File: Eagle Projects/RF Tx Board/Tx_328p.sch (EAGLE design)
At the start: 46 parts, among them Q3 16MHz, Q4 16MHz, U1 ATMEGA328P_TQFP, U2 MCP2551

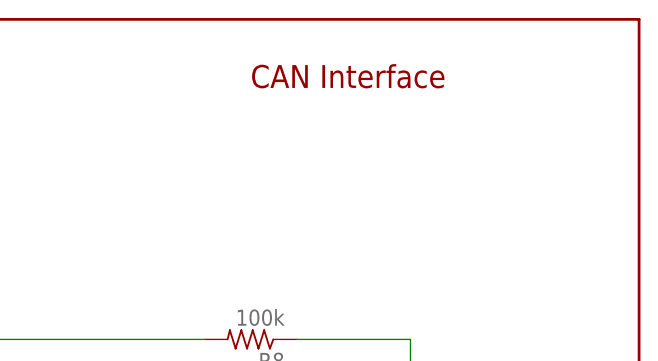
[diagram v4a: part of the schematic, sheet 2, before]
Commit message: Some routing done on Tx board
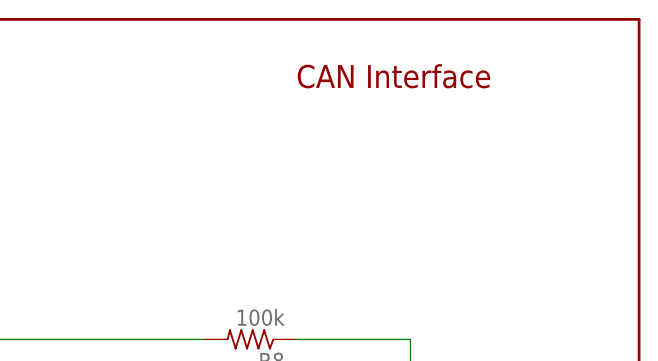
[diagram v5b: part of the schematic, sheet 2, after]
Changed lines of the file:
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@@
 <part name="S1" library="switch" deviceset="SKHMP*E010" device="" technology="S"/>
 <part name="RESET" library="SparkFun-Retired" deviceset="TAC_SWITCH" device="SMD" value="TAC_SWITCHSMD"/>
+<part name="VCC" library="pinhead" deviceset="PINHD-1X1" device=""/>
+<part name="GND" library="pinhead" deviceset="PINHD-1X1" device=""/>
+<part name="GND_2" library="pinhead" deviceset="PINHD-1X1" device=""/>
+<part name="VIN" library="pinhead" deviceset="PINHD-1X1" device=""/>
+<part name="GND16" library="supply1" deviceset="GND" device=""/>
+<part name="GND17" library="supply1" deviceset="GND" device=""/>
+<part name="P+13" library="supply1" deviceset="VCC" device=""/>
 <part name="U$1" library="RobThePyro" deviceset="MCP2515" device="SO"/>
 <part name="U2" library="SparkFun" deviceset="MCP2551" device=""/>
@@
 <part name="Z2" library="supressor" deviceset="TVS-UD-" device="SOD323"/>
 <part name="GND15" library="supply1" deviceset="GND" device=""/>
-<part name="VCC" library="pinhead" deviceset="PINHD-1X1" device=""/>
-<part name="GND" library="pinhead" deviceset="PINHD-1X1" device=""/>
-<part name="GND_2" library="pinhead" deviceset="PINHD-1X1" device=""/>
-<part name="VIN" library="pinhead" deviceset="PINHD-1X1" device=""/>
-<part name="GND16" library="supply1" deviceset="GND" device=""/>
-<part name="GND17" library="supply1" deviceset="GND" device=""/>
-<part name="P+13" library="supply1" deviceset="VCC" device=""/>
 </parts>
 <sheets>
@@
 <wire x1="119.38" y1="-30.48" x2="119.38" y2="60.96" width="0.3048" layer="94"/>
 <wire x1="119.38" y1="60.96" x2="-58.42" y2="60.96" width="0.3048" layer="94"/>
-<text x="76.2" y="53.34" size="2.54" layer="94">CAN Interface</text>
+<text x="81.28" y="53.34" size="2.54" layer="94">CAN Interface</text>
 </plain>
 <instances>

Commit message: Tidy up both boards
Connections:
- net +5V: no longer C7.2, C8.2, R4.2, R5.2, R6.2, U$1G$2.VDD, U2.VDD
- net VCC: now also C7.2, C8.2, R4.2, R5.2, R6.2, U$1G$2.VDD, U2.VDD

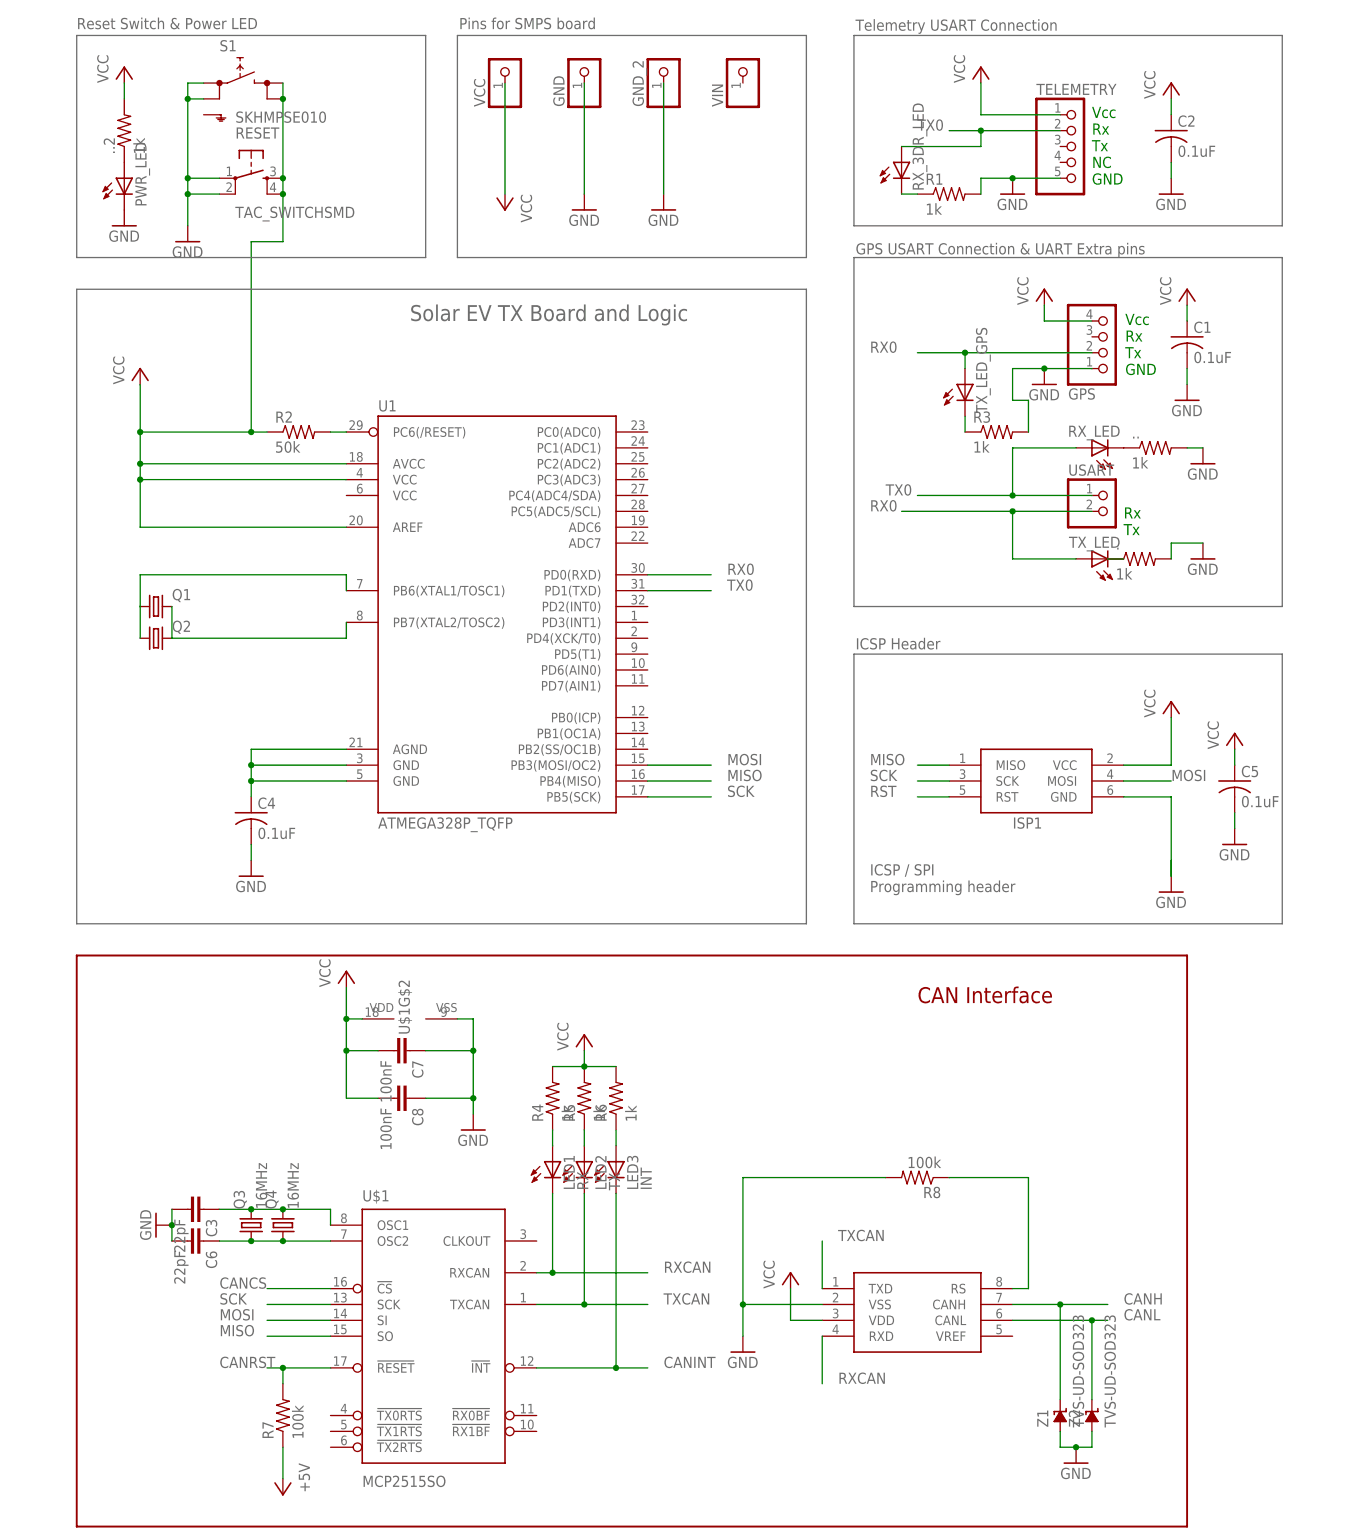
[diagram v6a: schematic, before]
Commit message: More board edits, nearly done routing (actual neatness is debatable)
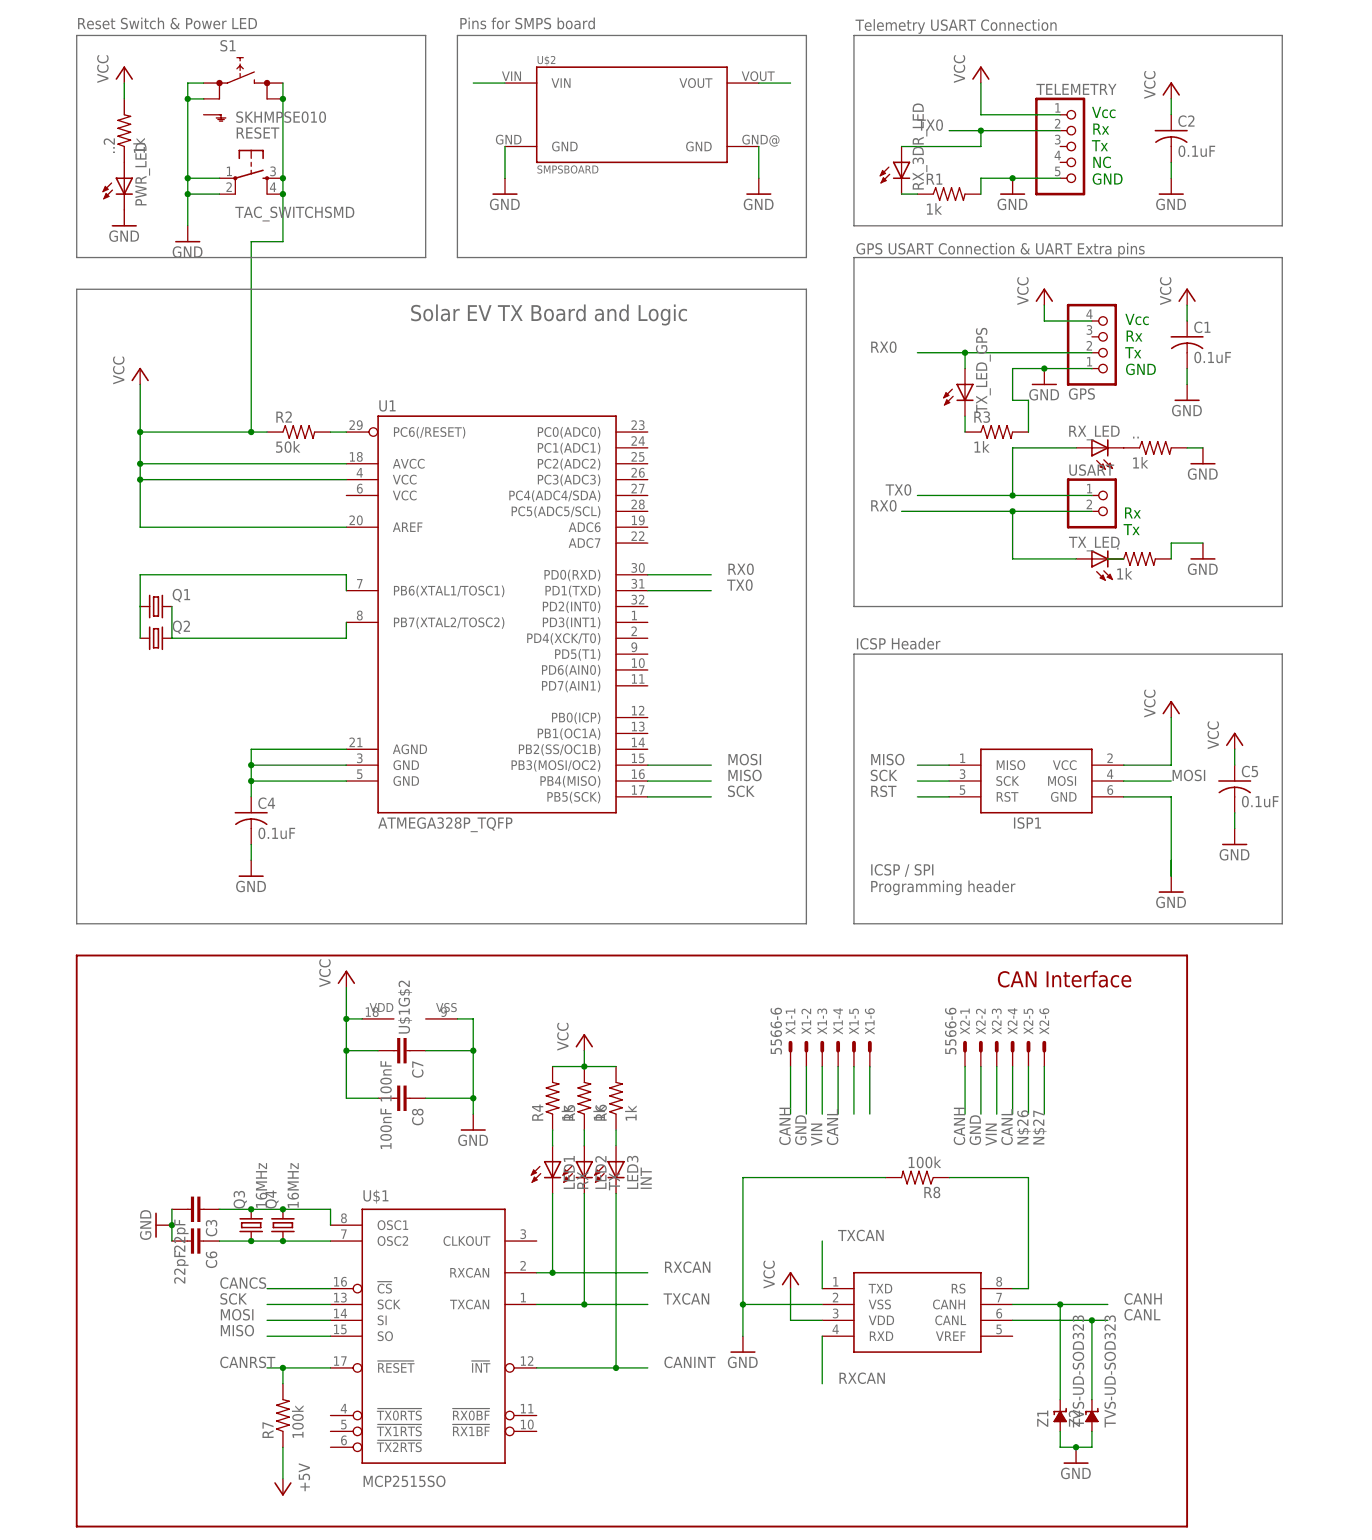
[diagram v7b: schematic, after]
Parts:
- removed GND, GND_2, VCC, VIN: (no value), pinhead:PINHD-1X1
- added U$2: SMPSBOARD, RobThePyro:SMPSBOARD
- added X1, X2: 5566-6, con-molex:5566-6
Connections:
- new net N$20: X1-5.S
- new net N$21: X1-6.S
- new net N$26: X2-5.S
- new net N$27: X2-6.S
- new net VIN: U$2.VIN, X1-3.S, X2-3.S
- net CANH: now also X1-1.S, X2-1.S
- net CANL: now also X1-4.S, X2-4.S
- net GND: now also U$2.GND, U$2.GND@1, X1-2.S, X2-2.S; no longer GND.1, GND_2.1
- net VCC: now also U$2.VOUT; no longer VCC.1
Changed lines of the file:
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@@
 <part name="S1" library="switch" deviceset="SKHMP*E010" device="" technology="S"/>
 <part name="RESET" library="SparkFun-Retired" deviceset="TAC_SWITCH" device="SMD" value="TAC_SWITCHSMD"/>
-<part name="VCC" library="pinhead" deviceset="PINHD-1X1" device=""/>
-<part name="GND" library="pinhead" deviceset="PINHD-1X1" device=""/>
-<part name="GND_2" library="pinhead" deviceset="PINHD-1X1" device=""/>
-<part name="VIN" library="pinhead" deviceset="PINHD-1X1" device=""/>
-<part name="GND16" library="supply1" deviceset="GND" device=""/>
-<part name="GND17" library="supply1" deviceset="GND" device=""/>
-<part name="P+13" library="supply1" deviceset="VCC" device=""/>
 <part name="U$1" library="RobThePyro" deviceset="MCP2515" device="SO"/>
 <part name="U2" library="SparkFun" deviceset="MCP2551" device=""/>
@@
 <part name="P+9" library="supply1" deviceset="VCC" device=""/>
 <part name="P+10" library="supply1" deviceset="VCC" device=""/>
+<part name="U$2" library="RobThePyro" deviceset="SMPSBOARD" device=""/>
+<part name="GND16" library="supply1" deviceset="GND" device=""/>
+<part name="GND17" library="supply1" deviceset="GND" device=""/>
+<part name="X1" library="con-molex" deviceset="5566-6" device=""/>
+<part name="X2" library="con-molex" deviceset="5566-6" device=""/>
 </parts>
 <sheets>
@@
 <wire x1="205.74" y1="-83.82" x2="205.74" y2="7.62" width="0.3048" layer="94"/>
 <wire x1="205.74" y1="7.62" x2="27.94" y2="7.62" width="0.3048" layer="94"/>
-<text x="162.56" y="0" size="2.54" layer="94">CAN Interface</text>
+<text x="175.26" y="2.54" size="2.54" layer="94">CAN Interface</text>
 </plain>
 <instances>
@@
 <instance part="S1" gate="G$1" x="53.34" y="147.32"/>
 <instance part="RESET" gate="S" x="55.88" y="132.08"/>
-<instance part="VCC" gate="G$1" x="96.52" y="149.86" rot="R90"/>
-<instance part="GND" gate="G$1" x="109.22" y="149.86" rot="R90"/>
-<instance part="GND_2" gate="G$1" x="121.92" y="149.86" rot="R90"/>
-<instance part="VIN" gate="G$1" x="134.62" y="149.86" rot="R90"/>
-<instance part="GND16" gate="1" x="121.92" y="127"/>
-<instance part="GND17" gate="1" x="109.22" y="127"/>
-<instance part="P+13" gate="VCC" x="96.52" y="127" rot="R180"/>
 <instance part="U$1" gate="G$1" x="86.36" y="-53.34"/>
 <instance part="U2" gate="G$1" x="157.48" y="-53.34"/>
@@
 <instance part="P+9" gate="VCC" x="109.22" y="-5.08"/>
 <instance part="P+10" gate="VCC" x="142.24" y="-43.18"/>
+<instance part="U$2" gate="G$1" x="116.84" y="142.24"/>
+<instance part="GND16" gate="1" x="96.52" y="129.54"/>
+<instance part="GND17" gate="1" x="137.16" y="129.54"/>
+<instance part="X1" gate="-1" x="142.24" y="-7.62" rot="R90"/>
+<instance part="X1" gate="-2" x="144.78" y="-7.62" rot="R90"/>
+<instance part="X1" gate="-3" x="147.32" y="-7.62" rot="R90"/>
+<instance part="X1" gate="-4" x="149.86" y="-7.62" rot="R90"/>
+<instance part="X1" gate="-5" x="152.4" y="-7.62" rot="R90"/>
+<instance part="X1" gate="-6" x="154.94" y="-7.62" rot="R90"/>
+<instance part="X2" gate="-1" x="170.18" y="-7.62" rot="R90"/>
+<instance part="X2" gate="-2" x="172.72" y="-7.62" rot="R90"/>
+<instance part="X2" gate="-3" x="175.26" y="-7.62" rot="R90"/>
+<instance part="X2" gate="-4" x="177.8" y="-7.62" rot="R90"/>
+<instance part="X2" gate="-5" x="180.34" y="-7.62" rot="R90"/>
+<instance part="X2" gate="-6" x="182.88" y="-7.62" rot="R90"/>
 </instances>
 <busses>
@@
 </segment>
 <segment>
-<pinref part="GND" gate="G$1" pin="1"/>
-<pinref part="GND17" gate="1" pin="GND"/>
-<wire x1="109.22" y1="147.32" x2="109.22" y2="129.54" width="0.1524" layer="91"/>
-</segment>
-<segment>
-<pinref part="GND_2" gate="G$1" pin="1"/>
-<pinref part="GND16" gate="1" pin="GND"/>
-<wire x1="121.92" y1="147.32" x2="121.92" y2="129.54" width="0.1524" layer="91"/>
-</segment>
-<segment>
 <pinref part="U2" gate="G$1" pin="VSS"/>
 <pinref part="GND13" gate="1" pin="GND"/>
@@
 <wire x1="43.18" y1="-35.56" x2="43.18" y2="-38.1" width="0.1524" layer="91"/>
 <junction x="43.18" y="-35.56"/>
+</segment>
+<segment>
+<pinref part="U$2" gate="G$1" pin="GND"/>
+<pinref part="GND16" gate="1" pin="GND"/>
+<wire x1="96.52" y1="137.16" x2="96.52" y2="132.08" width="0.1524" layer="91"/>
+</segment>
+<segment>
+<pinref part="U$2" gate="G$1" pin="GND@1"/>
+<pinref part="GND17" gate="1" pin="GND"/>
+<wire x1="137.16" y1="137.16" x2="137.16" y2="132.08" width="0.1524" layer="91"/>
+</segment>
+<segment>
+<wire x1="144.78" y1="-10.16" x2="144.78" y2="-17.78" width="0.1524" layer="91"/>
+<label x="144.78" y="-22.86" size="1.778" layer="95" rot="R90"/>
+<pinref part="X1" gate="-2" pin="S"/>
+</segment>
+<segment>
+<wire x1="172.72" y1="-10.16" x2="172.72" y2="-17.78" width="0.1524" layer="91"/>
+<label x="172.72" y="-22.86" size="1.778" layer="95" rot="R90"/>
+<pinref part="X2" gate="-2" pin="S"/>
 </segment>
 </net>
@@
 </segment>
 <segment>
-<pinref part="VCC" gate="G$1" pin="1"/>
-<pinref part="P+13" gate="VCC" pin="VCC"/>
-<wire x1="96.52" y1="147.32" x2="96.52" y2="129.54" width="0.1524" layer="91"/>
-</segment>
-<segment>
 <pinref part="U$1" gate="G$2" pin="VDD"/>
 <wire x1="73.66" y1="-2.54" x2="71.12" y2="-2.54" width="0.1524" layer="91"/>
@@
 <wire x1="142.24" y1="-50.8" x2="142.24" y2="-45.72" width="0.1524" layer="91"/>
 </segment>
+<segment>
+<pinref part="U$2" gate="G$1" pin="VOUT"/>
+<wire x1="137.16" y1="147.32" x2="142.24" y2="147.32" width="0.1524" layer="91"/>
+</segment>
 </net>
 <net name="N$9" class="0">
@@
 <junction x="185.42" y="-48.26"/>
 </segment>
+<segment>
+<wire x1="142.24" y1="-10.16" x2="142.24" y2="-17.78" width="0.1524" layer="91"/>
+<label x="142.24" y="-22.86" size="1.778" layer="95" rot="R90"/>
+<pinref part="X1" gate="-1" pin="S"/>
+</segment>
+<segment>
+<wire x1="170.18" y1="-10.16" x2="170.18" y2="-17.78" width="0.1524" layer="91"/>
+<label x="170.18" y="-22.86" size="1.778" layer="95" rot="R90"/>
+<pinref part="X2" gate="-1" pin="S"/>
+</segment>
 </net>
 <net name="CANL" class="0">
@@
 <wire x1="190.5" y1="-50.8" x2="193.04" y2="-50.8" width="0.1524" layer="91"/>
 <junction x="190.5" y="-50.8"/>
+</segment>
+<segment>
+<wire x1="149.86" y1="-10.16" x2="149.86" y2="-17.78" width="0.1524" layer="91"/>
+<label x="149.86" y="-22.86" size="1.778" layer="95" rot="R90"/>
+<pinref part="X1" gate="-4" pin="S"/>
+</segment>
+<segment>
+<wire x1="177.8" y1="-10.16" x2="177.8" y2="-17.78" width="0.1524" layer="91"/>
+<label x="177.8" y="-22.86" size="1.778" layer="95" rot="R90"/>
+<pinref part="X2" gate="-4" pin="S"/>
 </segment>
 </net>
@@
 </segment>
 </net>
+<net name="VIN" class="0">
+<segment>
+<pinref part="U$2" gate="G$1" pin="VIN"/>
+<wire x1="96.52" y1="147.32" x2="91.44" y2="147.32" width="0.1524" layer="91"/>
+</segment>
+<segment>
+<wire x1="147.32" y1="-10.16" x2="147.32" y2="-17.78" width="0.1524" layer="91"/>
+<label x="147.32" y="-22.86" size="1.778" layer="95" rot="R90"/>
+<pinref part="X1" gate="-3" pin="S"/>
+</segment>
+<segment>
+<wire x1="175.26" y1="-10.16" x2="175.26" y2="-17.78" width="0.1524" layer="91"/>
+<label x="175.26" y="-22.86" size="1.778" layer="95" rot="R90"/>
+<pinref part="X2" gate="-3" pin="S"/>
+</segment>
+</net>
+<net name="N$20" class="0">
+<segment>
+<wire x1="152.4" y1="-10.16" x2="152.4" y2="-17.78" width="0.1524" layer="91"/>
+<pinref part="X1" gate="-5" pin="S"/>
+</segment>
+</net>
+<net name="N$21" class="0">
+<segment>
+<wire x1="154.94" y1="-10.16" x2="154.94" y2="-17.78" width="0.1524" layer="91"/>
+<pinref part="X1" gate="-6" pin="S"/>
+</segment>
+</net>
+<net name="N$26" class="0">
+<segment>
+<wire x1="180.34" y1="-10.16" x2="180.34" y2="-17.78" width="0.1524" layer="91"/>
+<label x="180.34" y="-22.86" size="1.778" layer="95" rot="R90"/>
+<pinref part="X2" gate="-5" pin="S"/>
+</segment>
+</net>
+<net name="N$27" class="0">
+<segment>
+<wire x1="182.88" y1="-10.16" x2="182.88" y2="-17.78" width="0.1524" layer="91"/>
+<label x="182.88" y="-22.86" size="1.778" layer="95" rot="R90"/>
+<pinref part="X2" gate="-6" pin="S"/>
+</segment>
+</net>
